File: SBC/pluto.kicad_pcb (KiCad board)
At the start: 4 copper layers, 181.6 x 113 mm, 55 parts, among them J1 VIA1PA, J2 VIA1PB, J3 VIA2PB, J4 POWER, J5 VIA2PA, J6 RS232a, J7 RS232b, J8 JTAG, J9 TEST_2P, P1 IDE0, Q1 DS1813, SW1 RESET, U1 WD65C02PLCC44, U19 74LS574, U2 28C256, U20 74LS574, U21 74HC245, U22 MAX238, U23 SC28L92PLCC44, U3 AS6C62256A, U4 DS1511Y+, U5 WD65C22PLCC44, U6 WD65C22PLCC44, U7 ispMACH4A5, U8 74HC74, X1 8 MHz, X2 3.6864MHz

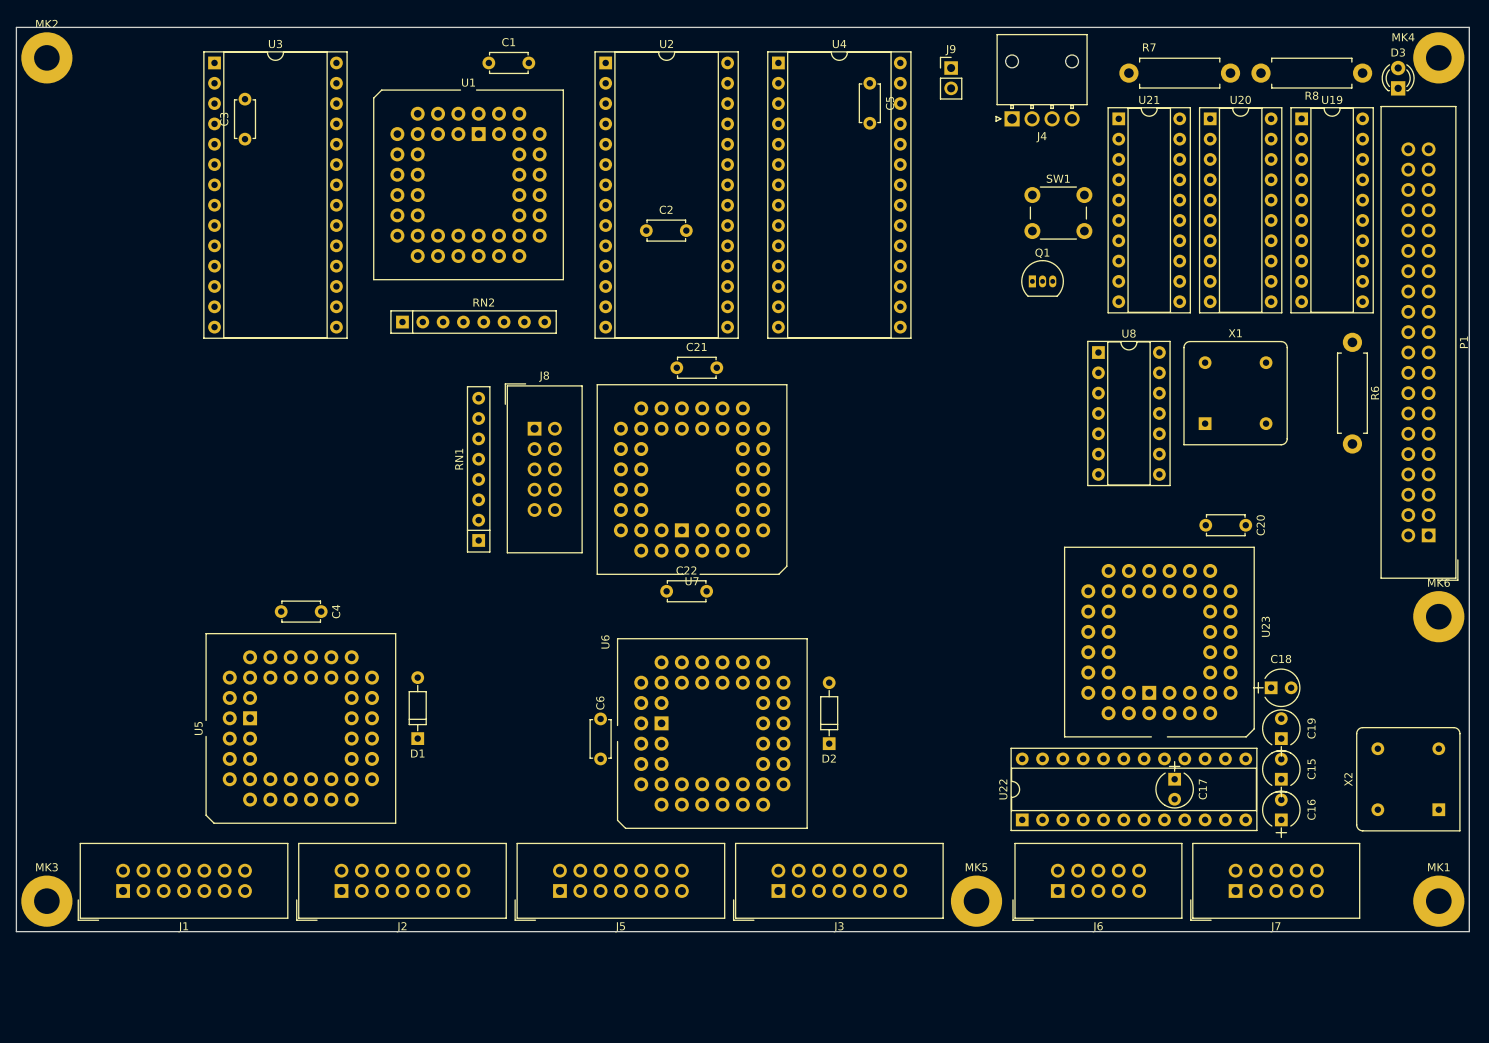
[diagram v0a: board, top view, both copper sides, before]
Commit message: Board ready for production. Added a reset IC that does both low and high logic RES. A power switch and fuse holder is in place. The expansion bus is back, but with an IDC 40 pin connector.
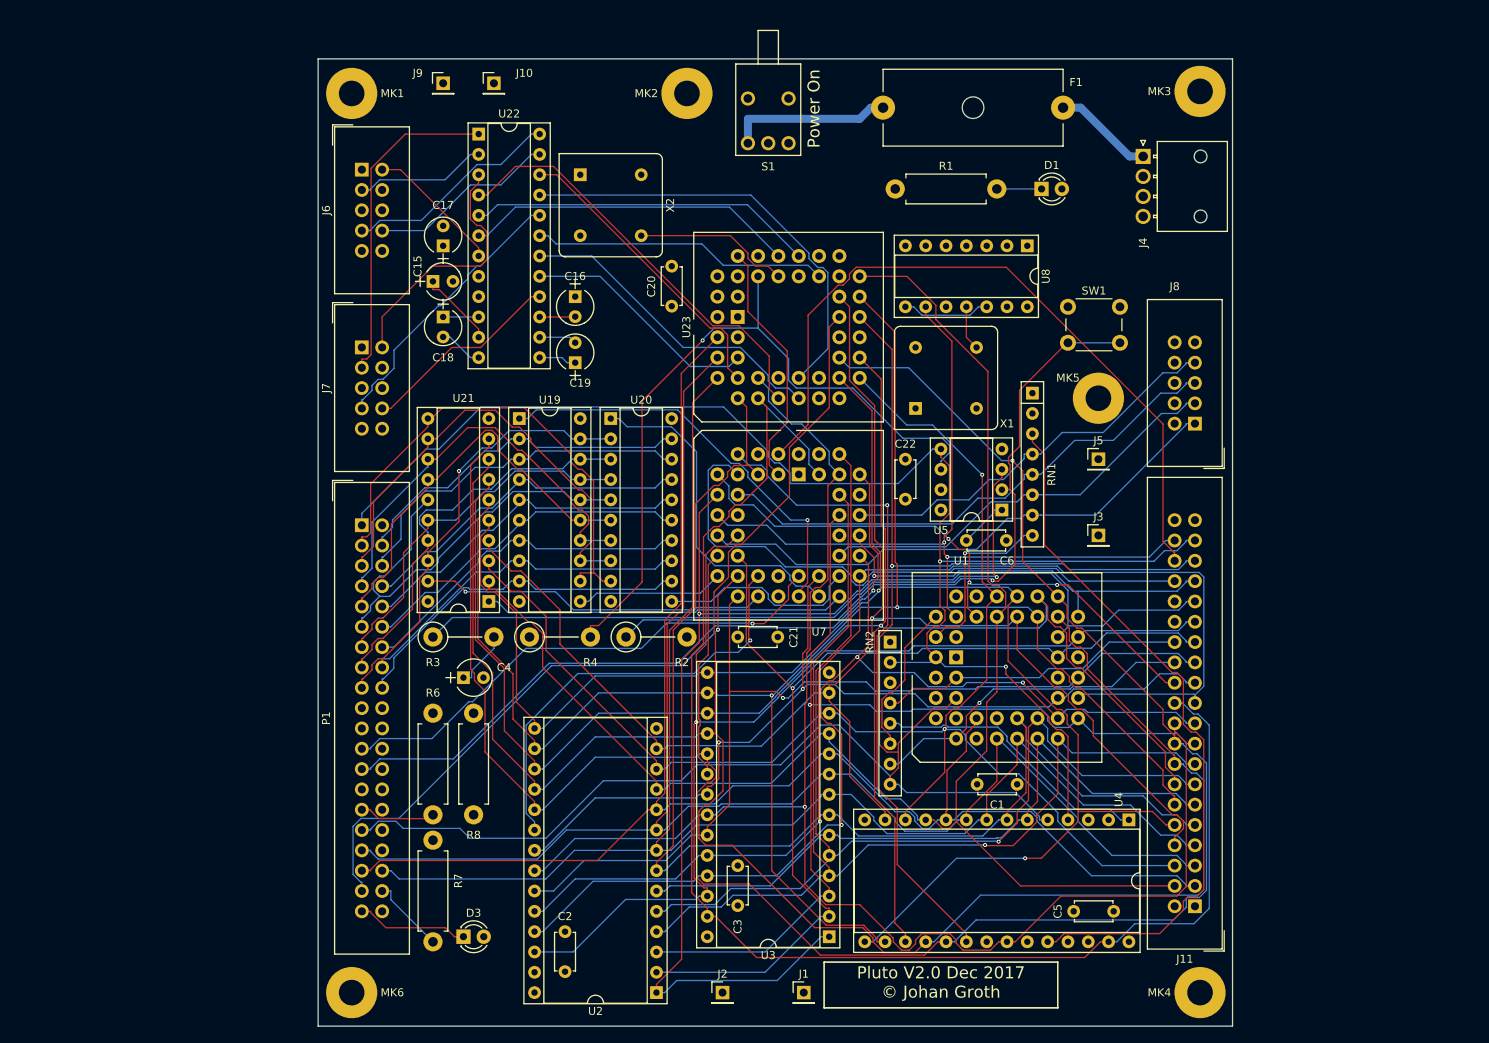
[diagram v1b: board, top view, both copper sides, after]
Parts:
- removed D2: D, Diodes_ThroughHole:D_DO-35_SOD27_P7.62mm_Horizontal
- removed Q1: DS1813, TO_SOT_Packages_THT:TO-92_Inline_Narrow_Oval
- removed U6: WD65C22PLCC44, Housings_LCC:PLCC-44_THT-Socket
- added F1: 1Amp, Fuse_Holders_and_Fuses:Fuseholder5x20_horiz_open_Schurter_0031_8201, F.Cu at (124.8, 25.9)
- added J10: GND3, Pin_Headers:Pin_Header_Straight_1x01_Pitch2.54mm, F.Cu at (76.2, 22.9)
- added J11: Expansion Bus, Connectors_IDC:IDC-Header_2x20_Pitch2.54mm_Straight, F.Cu at (163.8, 125.7)
- added R1: 1kOhm, Resistors_ThroughHole:R_Axial_DIN0411_L9.9mm_D3.6mm_P12.70mm_Horizontal, F.Cu at (126.4, 36.1)
- added R2: 22k, Resistors_ThroughHole:R_Axial_DIN0411_L9.9mm_D3.6mm_P7.62mm_Vertical, F.Cu at (92.7, 92.1)
- added R3: 475, Resistors_ThroughHole:R_Axial_DIN0411_L9.9mm_D3.6mm_P7.62mm_Vertical, F.Cu at (68.6, 92.1)
- added R4: 3.3k, Resistors_ThroughHole:R_Axial_DIN0411_L9.9mm_D3.6mm_P7.62mm_Vertical, F.Cu at (80.6, 92.1)
- added S1: SPDT, Switches_THT:SW-SPDT-0900766b81587629, F.Cu at (110.5, 27.3)
- C4: value 0.1uF -> 15uF; footprint Capacitors_ThroughHole:C_Disc_D4.7mm_W2.5mm_P5.00mm -> Capacitors_ThroughHole:CP_Radial_Tantal_D4.5mm_P2.50mm
- D1: value D -> LED; footprint Diodes_ThroughHole:D_DO-35_SOD27_P7.62mm_Horizontal -> LEDs:LED_D3.0mm
- J1: value VIA1PA -> VCC1; footprint Connectors_IDC:IDC-Header_2x07_Pitch2.54mm_Straight -> Pin_Headers:Pin_Header_Straight_1x01_Pitch2.54mm
- J2: value VIA1PB -> GND1; footprint Connectors_IDC:IDC-Header_2x07_Pitch2.54mm_Straight -> Pin_Headers:Pin_Header_Straight_1x01_Pitch2.54mm
- J3: value VIA2PB -> VCC2; footprint Connectors_IDC:IDC-Header_2x07_Pitch2.54mm_Straight -> Pin_Headers:Pin_Header_Straight_1x01_Pitch2.54mm
- J5: value VIA2PA -> GND2; footprint Connectors_IDC:IDC-Header_2x07_Pitch2.54mm_Straight -> Pin_Headers:Pin_Header_Straight_1x01_Pitch2.54mm
- J9: value TEST_2P -> VCC3; footprint Pin_Headers:Pin_Header_Straight_1x02_Pitch2.54mm -> Pin_Headers:Pin_Header_Straight_1x01_Pitch2.54mm
- U5: value WD65C22PLCC44 -> TL7705B; footprint Housings_LCC:PLCC-44_THT-Socket -> Housings_DIP:DIP-8_W7.62mm_Socket
- moved MK3 176.1 mm to (164.5, 23.9)
- moved MK1 169.3 mm to (58.4, 24.1)
- moved D3 157.8 mm to (72.4, 129.5), turned to 0 degrees
- moved R7 147.4 mm to (68.6, 130.2), turned to 90 degrees
- moved R8 144.7 mm to (73.7, 114.3), turned to 90 degrees
- moved MK6 143.8 mm to (58.4, 136.5)
- moved U3 133.5 mm to (118.1, 129.5), turned to 180 degrees
- moved X2 133.5 mm to (87.0, 34.3), turned to 270 degrees
- moved P1 133.4 mm to (59.7, 78.1), turned to 0 degrees
- moved R6 129.2 mm to (68.6, 114.3), turned to 90 degrees
- moved J7 128.6 mm to (59.7, 55.9), turned to 0 degrees
- moved J6 125.3 mm to (59.7, 33.7), turned to 0 degrees
- moved C15 123.0 mm to (68.6, 47.6), turned to 0 degrees
- moved MK4 120.6 mm to (164.5, 136.5)
- moved U2 116.4 mm to (96.5, 136.5), turned to 180 degrees
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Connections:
- C4 pad 1: VCC -> Net-(C4-Pad1)
- C6 pad 1: VCC -> Net-(C6-Pad1)
- D1 pad 2: /16bit IDE interface/~IRQ -> VCC
- J1 pad 1: GND -> VCC
- J3 pad 1: GND -> VCC
- J4 pad 1: (no net) -> /Power and mounting holes/PWR_IN
- J4 pad 4: VCC -> Net-(J4-Pad4)
- J6 pad 1: (no net) -> Net-(J6-Pad1)
- J6 pad 10: (no net) -> Net-(J6-Pad10)
- J6 pad 4: (no net) -> Net-(J6-Pad4)
- J6 pad 6: (no net) -> Net-(J6-Pad6)
- J6 pad 9: (no net) -> Net-(J6-Pad9)
- J7 pad 1: (no net) -> Net-(J7-Pad1)
- J7 pad 10: (no net) -> Net-(J7-Pad10)
- J7 pad 4: (no net) -> Net-(J7-Pad4)
- J7 pad 6: (no net) -> Net-(J7-Pad6)
- J7 pad 9: (no net) -> Net-(J7-Pad9)
- J8 pad 10: (no net) -> Net-(J8-Pad10)
- J8 pad 9: (no net) -> Net-(J8-Pad9)
- P1 pad 20: (no net) -> Net-(P1-Pad20)
- P1 pad 21: (no net) -> /16bit IDE interface/DMARQ
- P1 pad 27: (no net) -> /16bit IDE interface/IORDY
- P1 pad 28: (no net) -> Net-(P1-Pad28)
- P1 pad 34: (no net) -> Net-(P1-Pad34)
- RN1 pad 2: (no net) -> Net-(RN1-Pad2)
- RN1 pad 3: (no net) -> /Address decoding and support section/~KS
- RN2 pad 3: /Address decoding and support section/~KS -> Net-(RN2-Pad3)
- SW1 pad 2: /16bit IDE interface/~RES -> Net-(R2-Pad1)
- U1 pad 12: (no net) -> Net-(U1-Pad12)
- U1 pad 2: (no net) -> Net-(U1-Pad2)
- U1 pad 4: (no net) -> Net-(U1-Pad4)
- U1 pad 43: (no net) -> Net-(U1-Pad43)
- U1 pad 6: (no net) -> Net-(U1-Pad6)
- U1 pad 8: (no net) -> Net-(U1-Pad8)
- U23 pad 1: (no net) -> Net-(U23-Pad1)
- U23 pad 15: (no net) -> Net-(U23-Pad15)
- U23 pad 16: (no net) -> Net-(U23-Pad16)
- U23 pad 17: (no net) -> Net-(U23-Pad17)
- U23 pad 23: (no net) -> Net-(U23-Pad23)
- U23 pad 3: (no net) -> Net-(U23-Pad3)
- U23 pad 30: (no net) -> Net-(U23-Pad30)
- U23 pad 31: (no net) -> Net-(U23-Pad31)
- U23 pad 34: (no net) -> Net-(U23-Pad34)
- U23 pad 37: (no net) -> Net-(U23-Pad37)
- U23 pad 41: (no net) -> Net-(U23-Pad41)
- U23 pad 42: (no net) -> Net-(U23-Pad42)
- U23 pad 43: (no net) -> Net-(U23-Pad43)
- U4 pad 23: (no net) -> Net-(U4-Pad23)
- U5 pad 1: GND -> Net-(C6-Pad1)
- U5 pad 2: Net-(J1-Pad3) -> Net-(R2-Pad1)
- U5 pad 3: Net-(J1-Pad4) -> Net-(R3-Pad1)
- U5 pad 4: Net-(J1-Pad5) -> GND
- U5 pad 5: Net-(J1-Pad6) -> /16bit IDE interface/~RES
- U5 pad 6: Net-(J1-Pad7) -> /Address decoding and support section/RES
- U5 pad 7: Net-(J1-Pad8) -> VCC
- U5 pad 8: Net-(J1-Pad9) -> VCC
- U7 pad 37: /Address decoding and support section/RES -> Net-(U7-Pad37)
- U7 pad 4: (no net) -> Net-(U7-Pad4)
- U7 pad 42: /16bit IDE interface/~RES -> Net-(U7-Pad42)
- U8 pad 5: (no net) -> Net-(U8-Pad5)
- U8 pad 6: (no net) -> Net-(U8-Pad6)
- X1 pad 1: (no net) -> Net-(X1-Pad1)
- X2 pad 1: (no net) -> Net-(X2-Pad1)
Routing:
- net /16bit IDE interface/D6: track 0.00 -> 260.5 mm
- net /16bit IDE interface/D7: track 0.00 -> 256.1 mm, vias 0 -> 1
- net /16bit IDE interface/D5: track 0.00 -> 223.3 mm, vias 0 -> 1
- net /16bit IDE interface/D4: track 0.00 -> 217.7 mm, vias 0 -> 2
- net /16bit IDE interface/~IRQ: track 0.00 -> 211.2 mm, vias 0 -> 1
- net /16bit IDE interface/D3: track 0.00 -> 205.0 mm, vias 0 -> 2
- net /16bit IDE interface/A0: track 0.00 -> 196.0 mm
- net /16bit IDE interface/D0: track 0.00 -> 194.8 mm
- net /16bit IDE interface/D2: track 0.00 -> 191.6 mm, vias 0 -> 1
- net /16bit IDE interface/A1: track 0.00 -> 189.8 mm
- net /16bit IDE interface/~RES: track 0.00 -> 186.1 mm, vias 0 -> 2
- net /Address decoding and support section/~MRD: track 0.00 -> 185.4 mm, vias 0 -> 1
- net /16bit IDE interface/A2: track 0.00 -> 185.3 mm
- net /16bit IDE interface/D1: track 0.00 -> 181.6 mm, vias 0 -> 2
- net /Address decoding and support section/~MWR: track 0.00 -> 179.2 mm
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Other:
- board size 181.6 x 113 mm -> 114.3 x 120.9 mm
- net class Default: clearance 0.2 -> 0.15; trace_width 0.25 -> 0.15; via_dia 0.6 -> 0.5; via_drill 0.4 -> 0.3
- net class GND: clearance 0.2 -> 0.15; trace_width 0.25 -> 0.15; via_dia 0.6 -> 0.5; via_drill 0.4 -> 0.3
- net class PWR_IN added: clearance 0.5, trace_width 1, via_dia 0.5, via_drill 0.3
- net class VCC: clearance 0.2 -> 0.15; trace_width 0.45 -> 0.15; via_dia 0.6 -> 0.5; via_drill 0.4 -> 0.3
- rule trace_clearance: 0.2 -> 0.15
- rule trace_min: 0.2 -> 0.15
- board text added: "Pluto V2.0 Dec 2017 © Johan Groth"
- board text added: "Power On"
